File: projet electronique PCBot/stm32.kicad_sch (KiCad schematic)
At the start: 6 parts, among them J1 Conn_ST_STDC14, U1 STM32G431KBT6

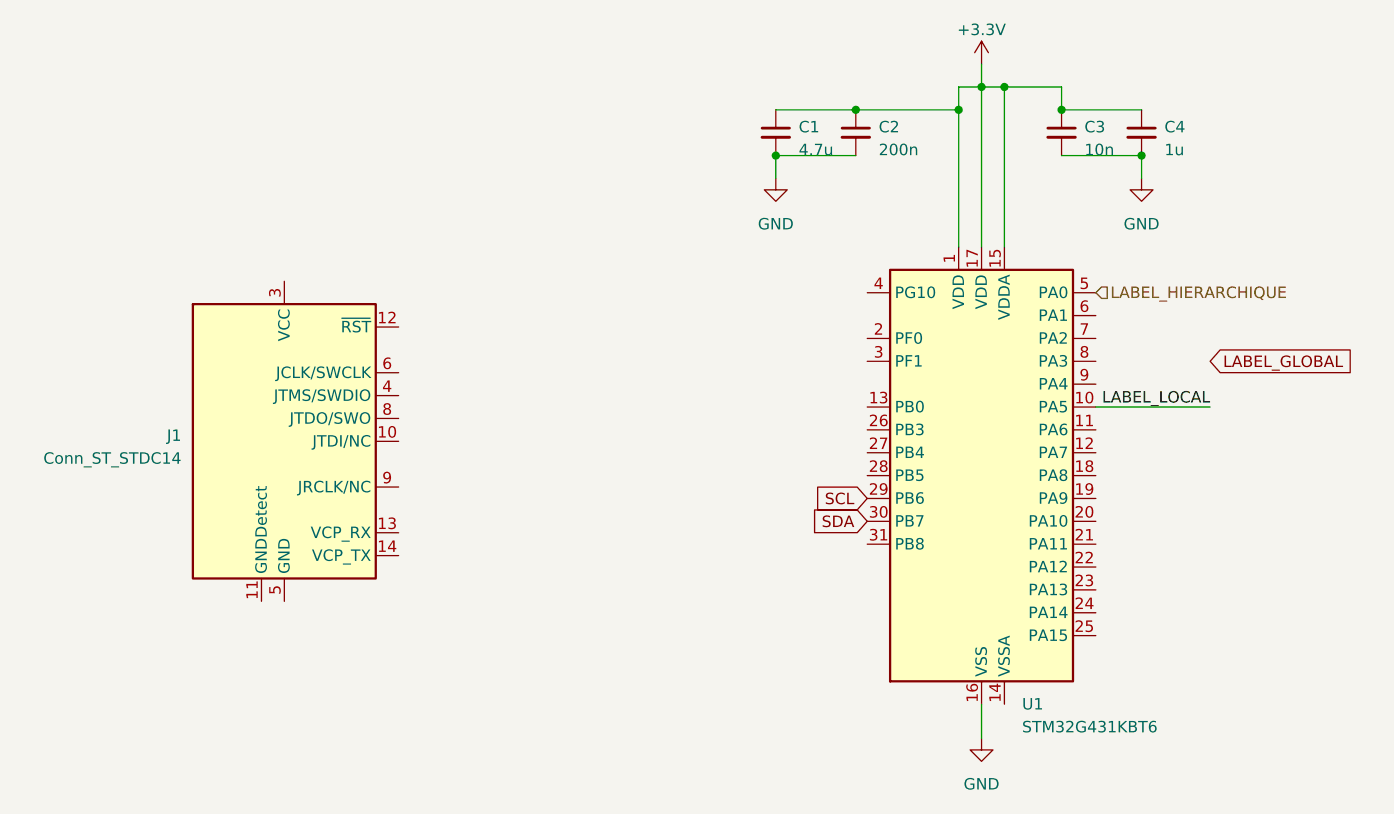
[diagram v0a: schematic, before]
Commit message: Modification des feuilles hiérarchiques et le main
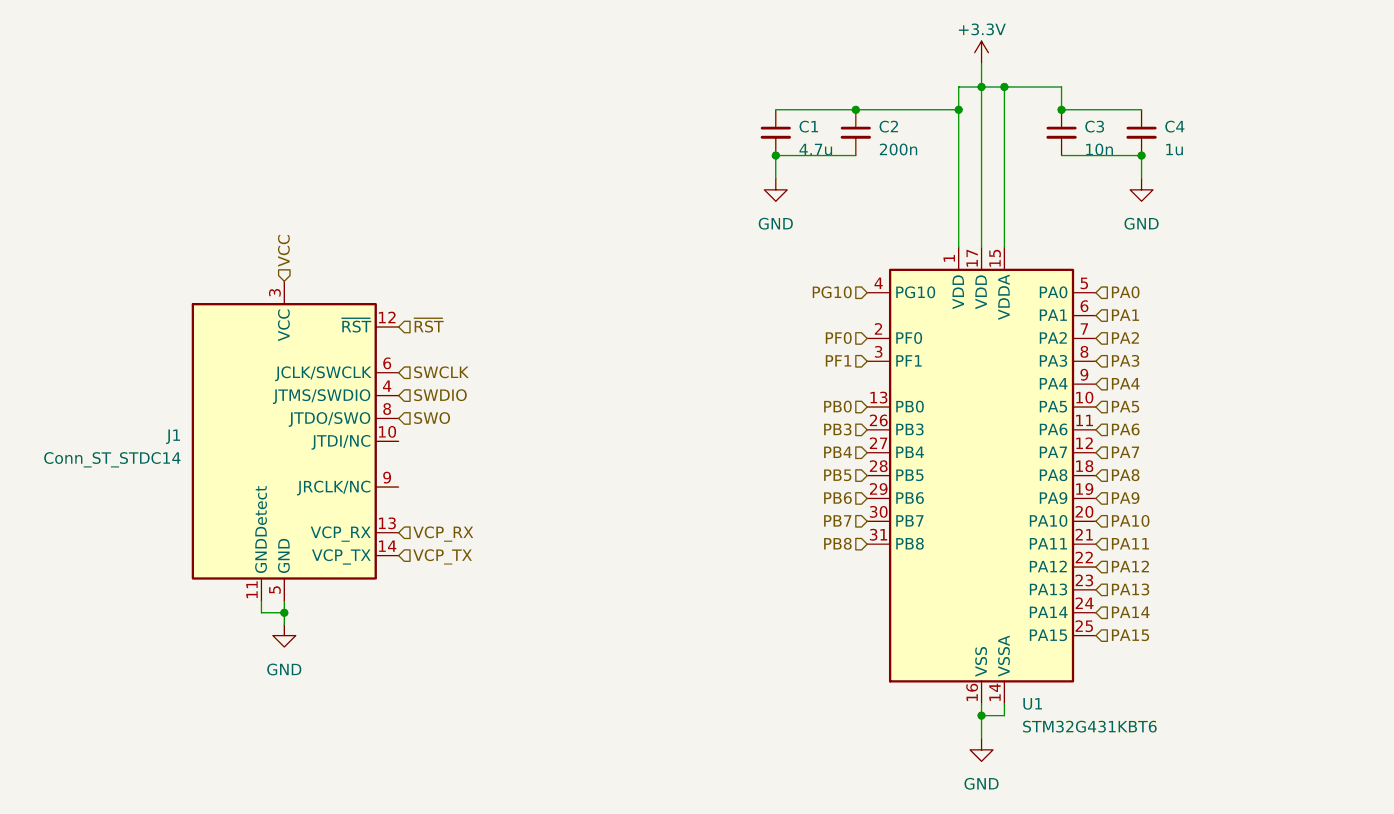
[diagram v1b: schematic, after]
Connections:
- net GND: now also J1.11 (GNDDetect), J1.5 (GND), J1.7 (GND), U1.14 (VSSA)
- net ~{RST}: now reaches J1.12 (~{RST})
- net VCP_RX: now reaches J1.13 (VCP_RX)
- net VCP_TX: now reaches J1.14 (VCP_TX)
- net VCC: now reaches J1.3 (VCC)
- net SWDIO: now reaches J1.4 (JTMS/SWDIO)
- net SWCLK: now reaches J1.6 (JCLK/SWCLK)
- net SWO: now reaches J1.8 (JTDO/SWO)
- net PA6: now reaches U1.11 (PA6)
- net PA7: now reaches U1.12 (PA7)
- net PB0: now reaches U1.13 (PB0)
- net PA8: now reaches U1.18 (PA8)
- net PA9: now reaches U1.19 (PA9)
- net PF0: now reaches U1.2 (PF0)
- net PA10: now reaches U1.20 (PA10)
- net PA11: now reaches U1.21 (PA11)
- net PA12: now reaches U1.22 (PA12)
- net PA13: now reaches U1.23 (PA13)
- net PA14: now reaches U1.24 (PA14)
- net PA15: now reaches U1.25 (PA15)
- net PB3: now reaches U1.26 (PB3)
- net PB4: now reaches U1.27 (PB4)
- net PB5: now reaches U1.28 (PB5)
- net PF1: now reaches U1.3 (PF1)
- net PB8: now reaches U1.31 (PB8)
- net PG10: now reaches U1.4 (PG10)
- net PA1: now reaches U1.6 (PA1)
- net PA2: now reaches U1.7 (PA2)
- net PA3: now reaches U1.8 (PA3)
- net PA4: now reaches U1.9 (PA4)
- net LABEL_HIERARCHIQUE renamed PA0
- net LABEL_LOCAL renamed PA5
- net SCL renamed PB6
- net SDA renamed PB7
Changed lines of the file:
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@@
   (junction (at 142.24 66.04) (diameter 0) (color 0 0 0 0)
   )
+  (junction (at 144.78 133.35) (diameter 0) (color 0 0 0 0)
+  )
   (junction (at 162.56 71.12) (diameter 0) (color 0 0 0 0)
   )
@@
   (junction (at 121.92 71.12) (diameter 0) (color 0 0 0 0)
   )
+  (junction (at 67.31 121.92) (diameter 0) (color 0 0 0 0)
+  )
   (junction (at 147.32 63.5) (diameter 0) (color 0 0 0 0)
   )
@@
     (stroke (width 0) (type default))
   )
+  (wire (pts (xy 147.32 132.08) (xy 147.32 133.35))
+    (stroke (width 0) (type default))
+  )
   (wire (pts (xy 142.24 63.5) (xy 144.78 63.5))
     (stroke (width 0) (type default))
   )
+  (wire (pts (xy 144.78 133.35) (xy 144.78 135.89))
+    (stroke (width 0) (type default))
+  )
   (wire (pts (xy 153.67 71.12) (xy 162.56 71.12))
     (stroke (width 0) (type default))
@@
     (stroke (width 0) (type default))
   )
+  (wire (pts (xy 64.77 120.65) (xy 64.77 121.92))
+    (stroke (width 0) (type default))
+  )
   (wire (pts (xy 142.24 81.28) (xy 142.24 66.04))
     (stroke (width 0) (type default))
@@
     (stroke (width 0) (type default))
   )
+  (wire (pts (xy 64.77 121.92) (xy 67.31 121.92))
+    (stroke (width 0) (type default))
+  )
   (wire (pts (xy 144.78 63.5) (xy 144.78 81.28))
     (stroke (width 0) (type default))
@@
     (stroke (width 0) (type default))
   )
+  (wire (pts (xy 67.31 121.92) (xy 67.31 123.19))
+    (stroke (width 0) (type default))
+  )
+  (wire (pts (xy 147.32 133.35) (xy 144.78 133.35))
+    (stroke (width 0) (type default))
+  )
   (wire (pts (xy 130.81 66.04) (xy 142.24 66.04))
     (stroke (width 0) (type default))
   )
-  (wire (pts (xy 170.18 99.06) (xy 157.48 99.06))
-    (stroke (width 0) (type default))
-  )
   (wire (pts (xy 153.67 66.04) (xy 162.56 66.04))
     (stroke (width 0) (type default))
   )
-  (wire (pts (xy 144.78 132.08) (xy 144.78 135.89))
+  (wire (pts (xy 144.78 132.08) (xy 144.78 133.35))
     (stroke (width 0) (type default))
   )
@@
     (stroke (width 0) (type default))
   )
-  (label "LABEL_LOCAL" (at 170.18 99.06 180) (fields_autoplaced)
-    (effects (font (size 1.27 1.27)) (justify right bottom))
-  )
-  (global_label "SDA" (shape input) (at 132.08 111.76 180) (fields_autoplaced)
-    (effects (font (size 1.27 1.27)) (justify right))
-    (property "Intersheetrefs" "${INTERSHEET_REFS}" (at 125.6061 111.76 0)
-      (effects (font (size 1.27 1.27)) (justify right) hide)
-    )
-  )
-  (global_label "LABEL_GLOBAL" (shape input) (at 170.18 93.98 0) (fields_autoplaced)
-    (effects (font (size 1.27 1.27)) (justify left))
-    (property "Intersheetrefs" "${INTERSHEET_REFS}" (at 186.6325 93.98 0)
-      (effects (font (size 1.27 1.27)) (justify left) hide)
-    )
-  )
-  (global_label "SCL" (shape input) (at 132.08 109.22 180) (fields_autoplaced)
-    (effects (font (size 1.27 1.27)) (justify right))
-    (property "Intersheetrefs" "${INTERSHEET_REFS}" (at 125.6666 109.22 0)
-      (effects (font (size 1.27 1.27)) (justify right) hide)
-    )
-  )
-  (hierarchical_label "LABEL_HIERARCHIQUE" (shape input) (at 157.48 86.36 0) (fields_autoplaced)
+  (wire (pts (xy 67.31 120.65) (xy 67.31 121.92))
+    (stroke (width 0) (type default))
+  )
+  (hierarchical_label "PB4" (shape input) (at 132.08 104.14 180) (fields_autoplaced)
+    (effects (font (size 1.27 1.27)) (justify right))
+  )
+  (hierarchical_label "~{RST}" (shape input) (at 80.01 90.17 0) (fields_autoplaced)
+    (effects (font (size 1.27 1.27)) (justify left))
+  )
+  (hierarchical_label "PA14" (shape input) (at 157.48 121.92 0) (fields_autoplaced)
+    (effects (font (size 1.27 1.27)) (justify left))
+  )
+  (hierarchical_label "PA15" (shape input) (at 157.48 124.46 0) (fields_autoplaced)
+    (effects (font (size 1.27 1.27)) (justify left))
+  )
+  (hierarchical_label "SWCLK" (shape input) (at 80.01 95.25 0) (fields_autoplaced)
+    (effects (font (size 1.27 1.27)) (justify left))
+  )
+  (hierarchical_label "PB3" (shape input) (at 132.08 101.6 180) (fields_autoplaced)
+    (effects (font (size 1.27 1.27)) (justify right))
+  )
+  (hierarchical_label "PF1" (shape input) (at 132.08 93.98 180) (fields_autoplaced)
+    (effects (font (size 1.27 1.27)) (justify right))
+  )
+  (hierarchical_label "VCP_RX" (shape input) (at 80.01 113.03 0) (fields_autoplaced)
+    (effects (font (size 1.27 1.27)) (justify left))
+  )
+  (hierarchical_label "PB7" (shape input) (at 132.08 111.76 180) (fields_autoplaced)
+    (effects (font (size 1.27 1.27)) (justify right))
+  )
+  (hierarchical_label "PA9" (shape input) (at 157.48 109.22 0) (fields_autoplaced)
+    (effects (font (size 1.27 1.27)) (justify left))
+  )
+  (hierarchical_label "PA0" (shape input) (at 157.48 86.36 0) (fields_autoplaced)
+    (effects (font (size 1.27 1.27)) (justify left))
+  )
+  (hierarchical_label "SWO" (shape input) (at 80.01 100.33 0) (fields_autoplaced)
+    (effects (font (size 1.27 1.27)) (justify left))
+  )
+  (hierarchical_label "SWDIO" (shape input) (at 80.01 97.79 0) (fields_autoplaced)
+    (effects (font (size 1.27 1.27)) (justify left))
+  )
+  (hierarchical_label "PA1" (shape input) (at 157.48 88.9 0) (fields_autoplaced)
+    (effects (font (size 1.27 1.27)) (justify left))
+  )
+  (hierarchical_label "VCC" (shape input) (at 67.31 85.09 90) (fields_autoplaced)
+    (effects (font (size 1.27 1.27)) (justify left))
+  )
+  (hierarchical_label "PG10" (shape input) (at 132.08 86.36 180) (fields_autoplaced)
+    (effects (font (size 1.27 1.27)) (justify right))
+  )
+  (hierarchical_label "PB6" (shape input) (at 132.08 109.22 180) (fields_autoplaced)
+    (effects (font (size 1.27 1.27)) (justify right))
+  )
+  (hierarchical_label "PF0" (shape input) (at 132.08 91.44 180) (fields_autoplaced)
+    (effects (font (size 1.27 1.27)) (justify right))
+  )
+  (hierarchical_label "PA8" (shape input) (at 157.48 106.68 0) (fields_autoplaced)
+    (effects (font (size 1.27 1.27)) (justify left))
+  )
+  (hierarchical_label "VCP_TX" (shape input) (at 80.01 115.57 0) (fields_autoplaced)
+    (effects (font (size 1.27 1.27)) (justify left))
+  )
+  (hierarchical_label "PA6" (shape input) (at 157.48 101.6 0) (fields_autoplaced)
+    (effects (font (size 1.27 1.27)) (justify left))
+  )
+  (hierarchical_label "PB5" (shape input) (at 132.08 106.68 180) (fields_autoplaced)
+    (effects (font (size 1.27 1.27)) (justify right))
+  )
+  (hierarchical_label "PB0" (shape input) (at 132.08 99.06 180) (fields_autoplaced)
+    (effects (font (size 1.27 1.27)) (justify right))
+  )
+  (hierarchical_label "PA12" (shape input) (at 157.48 116.84 0) (fields_autoplaced)
+    (effects (font (size 1.27 1.27)) (justify left))
+  )
+  (hierarchical_label "PB8" (shape input) (at 132.08 114.3 180) (fields_autoplaced)
+    (effects (font (size 1.27 1.27)) (justify right))
+  )
+  (hierarchical_label "PA4" (shape input) (at 157.48 96.52 0) (fields_autoplaced)
+    (effects (font (size 1.27 1.27)) (justify left))
+  )
+  (hierarchical_label "PA11" (shape input) (at 157.48 114.3 0) (fields_autoplaced)
+    (effects (font (size 1.27 1.27)) (justify left))
+  )
+  (hierarchical_label "PA10" (shape input) (at 157.48 111.76 0) (fields_autoplaced)
+    (effects (font (size 1.27 1.27)) (justify left))
+  )
+  (hierarchical_label "PA13" (shape input) (at 157.48 119.38 0) (fields_autoplaced)
+    (effects (font (size 1.27 1.27)) (justify left))
+  )
+  (hierarchical_label "PA3" (shape input) (at 157.48 93.98 0) (fields_autoplaced)
+    (effects (font (size 1.27 1.27)) (justify left))
+  )
+  (hierarchical_label "PA2" (shape input) (at 157.48 91.44 0) (fields_autoplaced)
+    (effects (font (size 1.27 1.27)) (justify left))
+  )
+  (hierarchical_label "PA5" (shape input) (at 157.48 99.06 0) (fields_autoplaced)
+    (effects (font (size 1.27 1.27)) (justify left))
+  )
+  (hierarchical_label "PA7" (shape input) (at 157.48 104.14 0) (fields_autoplaced)
     (effects (font (size 1.27 1.27)) (justify left))
   )
@@
         )
       )
+    )
+  )
+  (symbol (lib_id "power:GND") (at 67.31 123.19 0) (unit 1)
+    (in_bom yes) (on_board yes) (dnp no) (fields_autoplaced)
+    (property "Reference" "#PWR015" (at 67.31 129.54 0)
+      (effects (font (size 1.27 1.27)) hide)
+    )
+    (property "Value" "GND" (at 67.31 128.27 0)
+      (effects (font (size 1.27 1.27)))
+    )
+    (property "Footprint" "" (at 67.31 123.19 0)
+      (effects (font (size 1.27 1.27)) hide)
+    )
+    (property "Datasheet" "" (at 67.31 123.19 0)
+      (effects (font (size 1.27 1.27)) hide)
+    )
+    (pin "1")
+    (instances
+      (project "projet electronique PCBot"
+        (path "/210be09d-86cd-4faa-bb91-cc54c5972517/12710ea4-c2d3-4e50-951d-2a4a0058690c"
+          (reference "#PWR015") (unit 1)
+        )
+      )

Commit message: stm
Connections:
- net PA11 renamed TIM1_CH1N
- net PA12 renamed TIM1_CH2N
- net PA13 renamed SYS_JTMS-SWDIO
- net PA14 renamed SYS_JTCK-SWCLK
- net PA15 renamed USART2_RX
- net PA8 renamed TIM1_CH1
- net PA9 renamed TIM1_CH2
- net PB3 renamed USART2_TX
- net PB7 renamed I2C_SDA
- net PB8 renamed I2C_SCL
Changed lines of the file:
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@@
 		)
 	)
-	(hierarchical_label "PA14"
+	(hierarchical_label "SYS_JTCK-SWCLK"
 		(shape input)
 		(at 157.48 121.92 0)
@@
 		)
 	)
-	(hierarchical_label "PA15"
+	(hierarchical_label "USART2_RX"
 		(shape input)
 		(at 157.48 124.46 0)
@@
 		)
 	)
-	(hierarchical_label "PB3"
+	(hierarchical_label "USART2_TX"
 		(shape input)
 		(at 132.08 101.6 180)
@@
 		)
 	)
-	(hierarchical_label "PB7"
+	(hierarchical_label "I2C_SDA"
 		(shape input)
 		(at 132.08 111.76 180)
@@
 		)
 	)
-	(hierarchical_label "PA9"
+	(hierarchical_label "TIM1_CH2"
 		(shape input)
 		(at 157.48 109.22 0)
@@
 		)
 	)
-	(hierarchical_label "PA8"
+	(hierarchical_label "TIM1_CH1"
 		(shape input)
 		(at 157.48 106.68 0)
@@
 		)
 	)
-	(hierarchical_label "PA12"
+	(hierarchical_label "TIM1_CH2N"
 		(shape input)
 		(at 157.48 116.84 0)
@@
 		)
 	)
-	(hierarchical_label "PB8"
+	(hierarchical_label "I2C_SCL"
 		(shape input)
 		(at 132.08 114.3 180)
@@
 		)
 	)
-	(hierarchical_label "PA11"
+	(hierarchical_label "TIM1_CH1N"
 		(shape input)
 		(at 157.48 114.3 0)
@@
 		)
 	)
-	(hierarchical_label "PA13"
+	(hierarchical_label "SYS_JTMS-SWDIO"
 		(shape input)
 		(at 157.48 119.38 0)

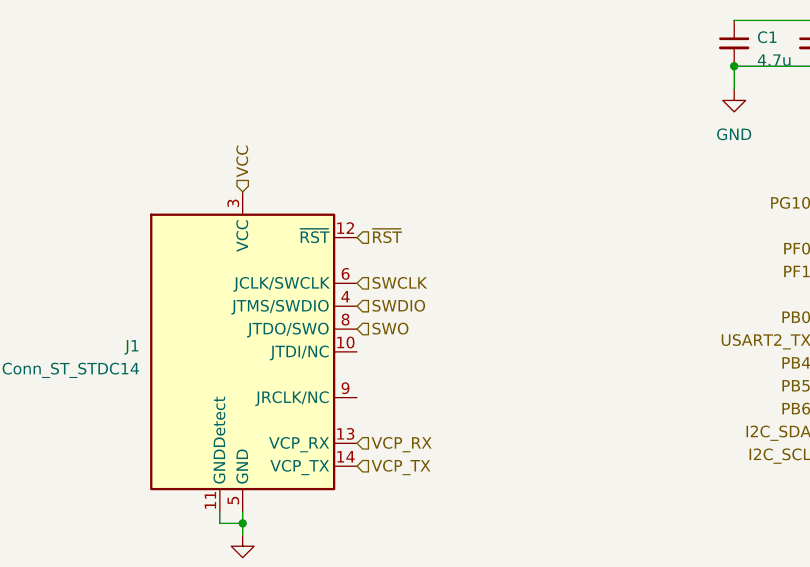
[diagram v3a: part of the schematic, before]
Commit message: modifications dans feuilles stm et capteurs
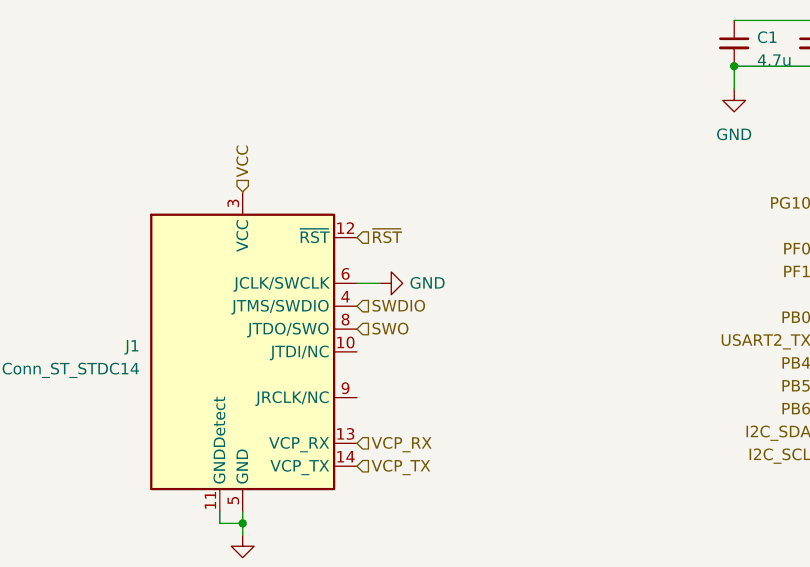
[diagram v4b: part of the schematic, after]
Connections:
- net SWCLK is gone; now on net GND: J1.6 (JCLK/SWCLK)
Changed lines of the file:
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@@
+	(wire
+		(pts
+			(xy 82.55 95.25) (xy 80.01 95.25)
+		)
+		(stroke
+			(width 0)
+			(type default)
+		)
+	)
 	(wire
 		(pts
@@
 		(shape input)
 		(at 157.48 124.46 0)
-		(effects
-			(font
-				(size 1.27 1.27)
-			)
-			(justify left)
-		)
-	)
-	(hierarchical_label "SWCLK"
-		(shape input)
-		(at 80.01 95.25 0)
 		(effects
 			(font
@@
 					(unit 1)
 				)
+			)
+		)
+	)
+	(symbol
+		(lib_name "GND_1")
+		(lib_id "power:GND")
+		(at 82.55 95.25 90)
+		(unit 1)
+		(exclude_from_sim no)
+		(in_bom yes)
+		(on_board yes)
+		(dnp no)
+		(property "Reference" "#PWR05"
+			(at 88.9 95.25 0)
+			(effects
+				(font
+					(size 1.27 1.27)
+				)
+				(hide yes)
+			)
+		)
+		(property "Value" "GND"
+			(at 85.852 95.25 90)
+			(effects
+				(font
+					(size 1.27 1.27)
+				)
+				(justify right)
+			)
+		)
+		(property "Footprint" ""
+			(at 82.55 95.25 0)
+			(effects
+				(font
+					(size 1.27 1.27)
+				)
+				(hide yes)
+			)
+		)
+		(property "Datasheet" ""
+			(at 82.55 95.25 0)
+			(effects
+				(font
+					(size 1.27 1.27)
+				)
+				(hide yes)
+			)
+		)
+		(property "Description" "Power symbol creates a global label with name \"GND\" , ground"
+			(at 82.55 95.25 0)
+			(effects
+				(font
+					(size 1.27 1.27)
+				)
+				(hide yes)
+			)
+		)
+		(pin "1"
+		)
+		(instances
+			(project ""
+				(path "/210be09d-86cd-4faa-bb91-cc54c5972517/12710ea4-c2d3-4e50-951d-2a4a0058690c"
+					(reference "#PWR05")
+					(unit 1)
+				)

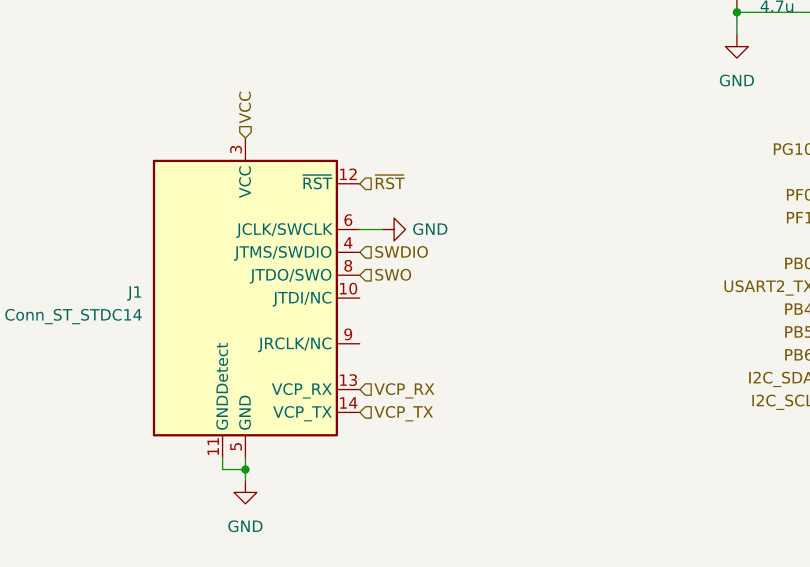
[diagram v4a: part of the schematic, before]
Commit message: suppression feuilles moteurs et connecteurs + modif feuille stm
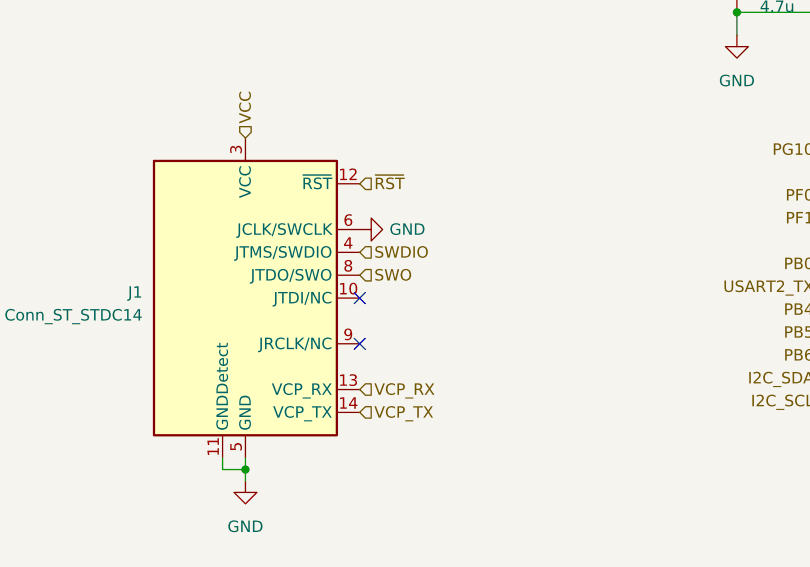
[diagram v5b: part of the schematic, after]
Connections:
- no-connect marks 0 -> 2
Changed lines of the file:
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@@
 		(color 0 0 0 0)
 	)
+	(no_connect
+		(at 80.01 102.87)
+	)
+	(no_connect
+		(at 80.01 107.95)
+	)
 	(wire
 		(pts
@@
 		(pts
 			(xy 144.78 133.35) (xy 144.78 135.89)
-		)
-		(stroke
-			(width 0)
-			(type default)
-		)
-	)
-	(wire
-		(pts
-			(xy 82.55 95.25) (xy 80.01 95.25)
 		)
 		(stroke
@@
 		(lib_name "GND_1")
 		(lib_id "power:GND")
-		(at 82.55 95.25 90)
+		(at 80.01 95.25 90)
 		(unit 1)
 		(exclude_from_sim no)
@@
 		(dnp no)
 		(property "Reference" "#PWR05"
-			(at 88.9 95.25 0)
+			(at 86.36 95.25 0)
 			(effects
 				(font
@@
 		)
 		(property "Value" "GND"
-			(at 85.852 95.25 90)
+			(at 83.312 95.25 90)
 			(effects
 				(font
@@
 		)
 		(property "Footprint" ""
-			(at 82.55 95.25 0)
+			(at 80.01 95.25 0)
 			(effects
 				(font
@@
 		)
 		(property "Datasheet" ""
-			(at 82.55 95.25 0)
+			(at 80.01 95.25 0)
 			(effects
 				(font
@@
 		)
 		(property "Description" "Power symbol creates a global label with name \"GND\" , ground"
-			(at 82.55 95.25 0)
-			(effects
-				(font
+			(at 80.01 95.25 0)
+			(effects
+				(font
